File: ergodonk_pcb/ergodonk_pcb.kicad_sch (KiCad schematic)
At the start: 134 parts, among them J1 AudioJack4, Q1 TIP120, SW0 SW_PUSH_LED, SW08_RH10 SW_PUSH_LED, SW1 SW_PUSH_LED, SW10 SW_PUSH_LED, SW11 SW_PUSH_LED, SW12 SW_PUSH_LED, SW13 SW_PUSH_LED, SW14 SW_PUSH_LED, SW15 SW_PUSH_LED, SW16 SW_PUSH_LED, SW17 SW_PUSH_LED, SW18_RH10 SW_PUSH_LED, SW2 SW_PUSH_LED, SW20 SW_PUSH_LED, SW21 SW_PUSH_LED, SW22 SW_PUSH_LED, SW23 SW_PUSH_LED, SW24 SW_PUSH_LED, SW25 SW_PUSH_LED, SW26 SW_PUSH_LED, SW27 SW_PUSH_LED, SW28_RH10 SW_PUSH_LED, SW3 SW_PUSH_LED, SW30 SW_PUSH_LED, SW31 SW_PUSH_LED, SW32 SW_PUSH_LED, SW33 SW_PUSH_LED, SW34 SW_PUSH_LED, SW35 SW_PUSH_LED, SW36 SW_PUSH_LED, SW37 SW_PUSH_LED, SW38_RH10 SW_PUSH_LED, SW4 SW_PUSH_LED, SW40 SW_PUSH_LED, SW42 SW_PUSH_LED, SW43 SW_PUSH_LED, SW44 SW_PUSH_LED, SW45 SW_PUSH_LED, SW46 SW_PUSH_LED, SW47 SW_PUSH_LED, SW48_RH10 SW_PUSH_LED, SW5 SW_PUSH_LED, SW50 SW_PUSH_LED, SW51 SW_PUSH_LED, SW52 SW_PUSH_LED, SW53 SW_PUSH_LED, SW54 SW_PUSH_LED, SW55 SW_PUSH_LED, SW56 SW_PUSH_LED, SW57 SW_PUSH_LED, SW58 SW_PUSH_LED, SW6 SW_PUSH_LED, SW7 SW_PUSH_LED

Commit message: Removed hand indication pin pin and updated footprints
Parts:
- removed JP6: SolderJumper_3_Open, Keebio-Parts:SolderJumper, symbol Jumper:SolderJumper_3_Open
- D0, D08_RH10, D1, D10, D11, D12, D13, D14, D15, D16, D17, D18_RH10, D2, D20, D21, D22, D23, D24, D25, D26, D27, D28_RH10, D3, D30, D31, D32, D33, D34, D35, D36, D37, D38_RH10, D4, D40, D41, D42, D43, D44, D45, D46, D47, D48_RH10, D5, D50, D51, D52, D53, D54, D55, D56, D57, D58, D6, D7: footprint ergodonk_kicad_library:D3_TH_SMD_v3_ergodonk -> ergodonk_kicad_library:D_SOD-123_DO-35_Hybrid_DoubleSided
- Q1: footprint Package_TO_SOT_THT:TO-220-3_Vertical -> Package_TO_SOT_THT:TO-220-3_Horizontal_TabDown
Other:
- note added: "Todo: Unbridge the handed pin jumper before double sided Add 2mm border Rewire for ProMicro footprint RH trackball Double sided RH/LH Add LEDs Graphics Mouse bites Stabalizer holes Improve solenoid graphics Refactor key row/columns to put 00 in upper right for easier double sided Make Diode holes bigger Add breakaway diode bender jig, like on Corne_light v1"
- note removed: "Split hand pin. Left is high, right would be low."
- note removed: "Todo: Unbridge the handed pin jumper before double sided Add 2mm border Rewire for ProMicro footprint RH trackball Double sided RH/LH Add LEDs Graphics Mouse bites Stabalizer holes Improve solenoid graphics Refactor key row/columns to put 00 in upper right for easier double sided"

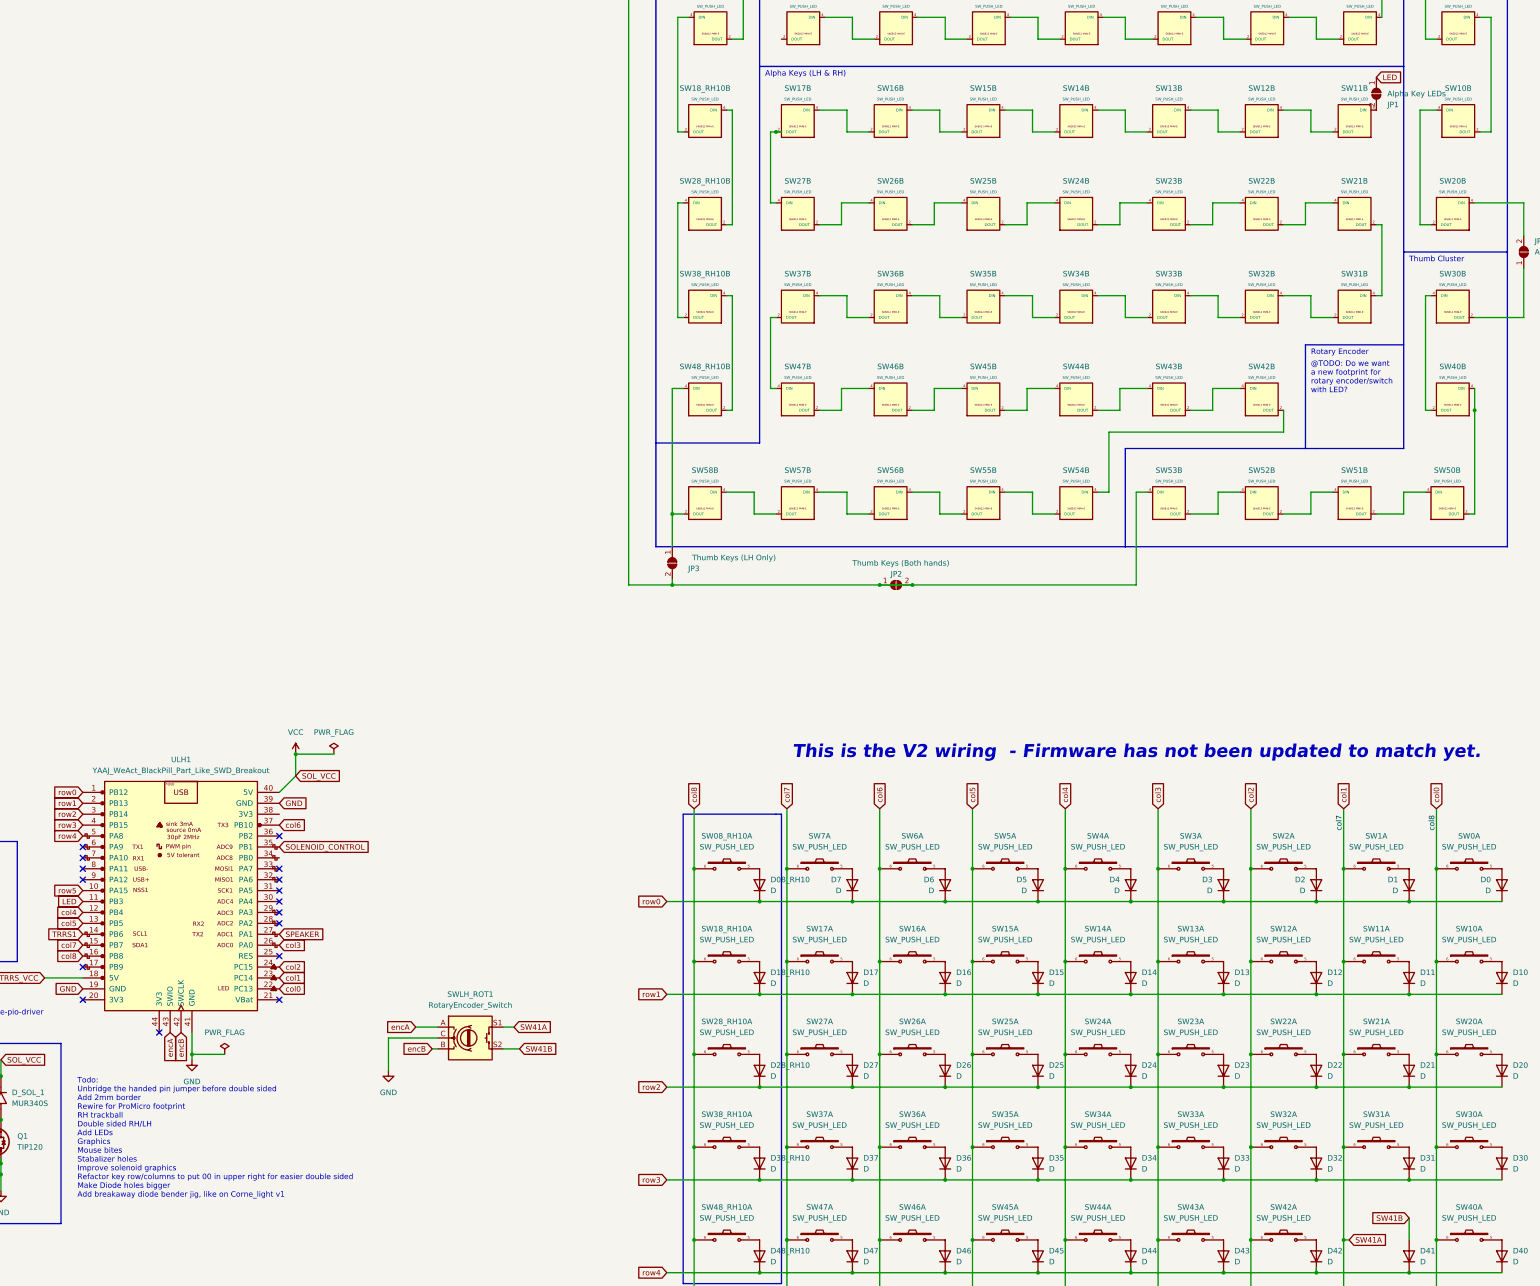
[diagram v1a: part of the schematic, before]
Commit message: Increased default net width and removed LED initial jumper
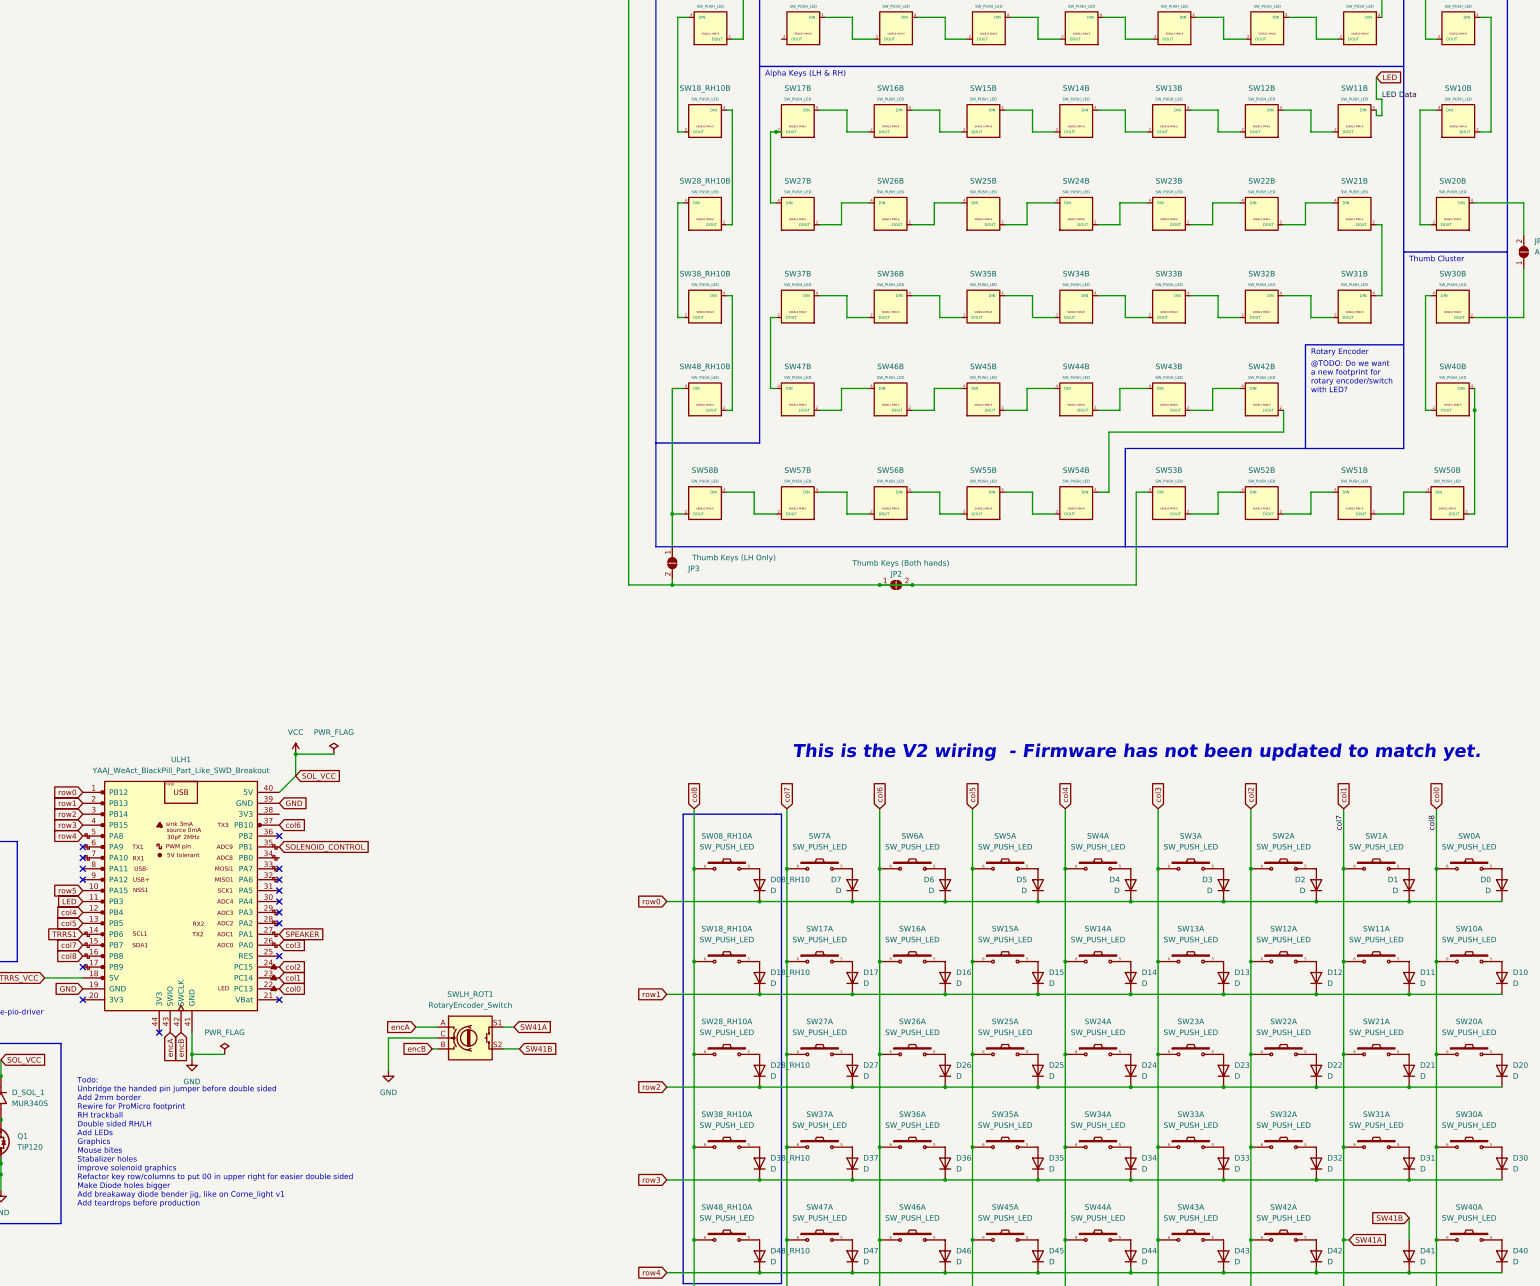
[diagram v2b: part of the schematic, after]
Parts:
- removed JP1: Alpha Key LEDs, Keebio-Parts:solder_jumper, symbol Jumper:SolderJumper_2_Open
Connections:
- net LED: now also SW11.4 (DIN)
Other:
- note added: "Todo: Unbridge the handed pin jumper before double sided Add 2mm border Rewire for ProMicro footprint RH trackball Double sided RH/LH Add LEDs Graphics Mouse bites Stabalizer holes Improve solenoid graphics Refactor key row/columns to put 00 in upper right for easier double sided Make Diode holes bigger Add breakaway diode bender jig, like on Corne_light v1 Add teardrops before production"
- note removed: "Todo: Unbridge the handed pin jumper before double sided Add 2mm border Rewire for ProMicro footprint RH trackball Double sided RH/LH Add LEDs Graphics Mouse bites Stabalizer holes Improve solenoid graphics Refactor key row/columns to put 00 in upper right for easier double sided Make Diode holes bigger Add breakaway diode bender jig, like on Corne_light v1"
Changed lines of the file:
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@@
     (stroke (width 0) (type default))
   )
+  (wire (pts (xy 373.38 -133.35) (xy 373.38 -129.54))
+    (stroke (width 0) (type default))
+  )
   (wire (pts (xy 299.72 45.72) (xy 299.72 31.75))
     (stroke (width 0) (type default))
@@
     (stroke (width 0) (type default))
   )
+  (wire (pts (xy 372.11 -133.35) (xy 372.11 -138.43))
+    (stroke (width 0) (type default))
+  )
   (wire (pts (xy 335.28 -82.55) (xy 335.28 -87.63))
     (stroke (width 0) (type default))
@@
     (stroke (width 0) (type default))
   )
+  (wire (pts (xy 373.38 -129.54) (xy 372.11 -129.54))
+    (stroke (width 0) (type default))
+  )
   (polyline (pts (xy 55.88 67.31) (xy 55.88 39.37))
     (stroke (width 0) (type default))
@@
     (stroke (width 0) (type default))
   )
+  (wire (pts (xy 372.11 -129.54) (xy 372.11 -130.81))
+    (stroke (width 0) (type default))
+  )
   (wire (pts (xy 290.83 -104.14) (xy 290.83 -109.22))
     (stroke (width 0) (type default))
@@
     (stroke (width 0) (type default))
   )
+  (wire (pts (xy 373.38 -133.35) (xy 372.11 -133.35))
+    (stroke (width 0) (type default))
+  )
   (wire (pts (xy 372.11 -104.14) (xy 373.38 -104.14))
     (stroke (width 0) (type default))
@@
     (effects (font (size 3 3) (thickness 0.6) bold italic) (justify left bottom))
   )
-  (text "Todo:\nUnbridge the handed pin jumper before double sided\nAdd 2mm border\nRewire for ProMicro footprint\nRH trackball\nDouble sided RH/LH\nAdd LEDs\nGraphics\nMouse bites\nStabalizer holes\nImprove solenoid graphics\nRefactor key row/columns to put 00 in upper right for easier double sided\nMake Diode holes bigger\nAdd breakaway diode bender jig, like on Corne_light v1\n\n"
+  (text "Todo:\nUnbridge the handed pin jumper before double sided\nAdd 2mm border\nRewire for ProMicro footprint\nRH trackball\nDouble sided RH/LH\nAdd LEDs\nGraphics\nMouse bites\nStabalizer holes\nImprove solenoid graphics\nRefactor key row/columns to put 00 in upper right for easier double sided\nMake Diode holes bigger\nAdd breakaway diode bender jig, like on Corne_light v1\nAdd teardrops before production\n"
     (at 69.85 124.46 0)
     (effects (font (size 1.27 1.27)) (justify left bottom))
@@
     (effects (font (size 1.27 1.27)) (justify left bottom))
   )
+  (label "LED Data" (at 373.38 -133.35 0) (fields_autoplaced)
+    (effects (font (size 1.27 1.27)) (justify left bottom))
+  )
   (label "col8" (at 386.08 36.83 90) (fields_autoplaced)
     (effects (font (size 1.27 1.27)) (justify left bottom))
@@
         )
       )
-    )
-  )
-  (symbol (lib_id "Jumper:SolderJumper_2_Open") (at 372.11 -134.62 270) (unit 1)
-    (in_bom yes) (on_board yes) (dnp no)
-    (property "Reference" "JP1" (at 374.65 -132.08 90)
-      (effects (font (size 1.27 1.27)) (justify left))
-    )
-    (property "Value" "Alpha Key LEDs" (at 374.65 -134.62 90)
-      (effects (font (size 1.27 1.27)) (justify left))
-    )
-    (property "Footprint" "Keebio-Parts:solder_jumper" (at 372.11 -134.62 0)
-      (effects (font (size 1.27 1.27)) hide)
-    )
-    (property "Datasheet" "~" (at 372.11 -134.62 0)
-      (effects (font (size 1.27 1.27)) hide)
-    )
-    (pin "1")
-    (pin "2")
-    (instances
-      (project "ergodonk_pcb"
-        (path "/ed1aaf15-4e1f-4159-b371-d99b3fb972ad"
-          (reference "JP1") (unit 1)
-        )
-      )

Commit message: Switch footprint refactor Hotswop outline replaced and rounded Hotswap pad numbering aligned per side Hotswap pad traces and vias added miniE led footprint with doublesided vias added Schematics updated PCB updated
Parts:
- SW0, SW1, SW10, SW11, SW12, SW13, SW14, SW15, SW16, SW17, SW2, SW20, SW21, SW22, SW23, SW24, SW25, SW26, SW3, SW30, SW31, SW32, SW33, SW34, SW35, SW36, SW4, SW40, SW42, SW43, SW44, SW45, SW46, SW5, SW50, SW54, SW55, SW56, SW6, SW7: footprint ergodonk_kicad_library:CherryMX_DoubleSided_Hotswap_miniE -> ergodonk_kicad_library:V2_CherryMX_DoubleSided_Hotswap_miniE
- SW08_RH10: footprint ergodonk_kicad_library:CherryMX_DoubleSided_Hotswap_miniE_2u_RH_ONLY -> ergodonk_kicad_library:V2_CherryMX_DoubleSided_Hotswap_miniE_2u_RH_ONLY
- SW18_RH10, SW38_RH10: footprint ergodonk_kicad_library:CherryMX_DoubleSided_Hotswap_miniE_1u_RH_ONLY -> ergodonk_kicad_library:V2_CherryMX_DS_Hotswap_miniE_1U_SEED_RH
- SW27: footprint ergodonk_kicad_library:CherryMX_DoubleSided_Hotswap_miniE_1.5u_LH_1u_RH -> ergodonk_kicad_library:V2_CherryMX_DoubleSided_Hotswap_miniE_1.5u_LH_1u_RH
- SW28_RH10: footprint ergodonk_kicad_library:CherryMX_DoubleSided_Hotswap_miniE_1.5u_RH_ONLY -> ergodonk_kicad_library:V2_CherryMX_DoubleSided_Hotswap_miniE_1.5u_RH_ONLY
- SW37: footprint ergodonk_kicad_library:CherryMX_DoubleSided_Hotswap_miniE_1.75u_LH_1u_RH -> ergodonk_kicad_library:V2_CherryMX_DoubleSided_Hotswap_miniE_1.75u_LH_1u_RH
- SW47: footprint ergodonk_kicad_library:CherryMX_DoubleSided_Hotswap_miniE_2.25u_LH_2.75u_RH -> ergodonk_kicad_library:V2_CherryMX_DoubleSided_Hotswap_miniE_2.25u_LH_2.75u_RH
- SW48_RH10: footprint ergodonk_kicad_library:CherryMX_DoubleSided_Hotswap_miniE_2.25u_LH_ONLY -> ergodonk_kicad_library:V2_CherryMX_DoubleSided_Hotswap_miniE_2.25u_LH_ONLY
- SW51, SW52: footprint ergodonk_kicad_library:CherryMX_DoubleSided_Hotswap_miniE_2u_Vertical -> ergodonk_kicad_library:V2_CherryMX_DoubleSided_Hotswap_miniE_2u_Vertical
- SW53: footprint ergodonk_kicad_library:CherryMX_DoubleSided_Hotswap_miniE_1.25u_Vertical -> ergodonk_kicad_library:V2_CherryMX_DoubleSided_Hotswap_miniE_1.25u_Vertical
- SW57, SW58: footprint ergodonk_kicad_library:CherryMX_DoubleSided_Hotswap_miniE_1.25u -> ergodonk_kicad_library:V2_CherryMX_DoubleSided_Hotswap_miniE_1.25u

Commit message: Rewired to 2040 begun Rewired rows and columns Added net names for rows and columns. Removed Key 00 to make room for PI Added OLED Added SDA/SDL breakout for optional Pimoroni
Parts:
- removed D0: D, ergodonk_kicad_library:D_SOD-123_DO-35_Hybrid_DoubleSided, symbol Device:D
- removed J1: AudioJack4, kbd:MJ-4PP-9, symbol kbd:MJ-4PP-9
- removed SW0: SW_PUSH_LED, ergodonk_kicad_library:V2_CherryMX_DoubleSided_Hotswap_miniE, symbol SofleKeyboard:SW_PUSH_LED
- added J10: TRRS Double Sided, Resistor_SMD:R_1206_3216Metric_Pad1.30x1.75mm_HandSolder, symbol Ergodonk_symbols:TRRS_TX_to_RX_Doublesided_Crossover
- added J12: Conn_01x04_Socket, symbol Connector:Conn_01x04_Socket
- added JP10: Jumper_2_Open, symbol Jumper:Jumper_2_Open
- added OL10: OLED, symbol kbd:OLED
- added R12: R, symbol Device:R
- added R2: 10k, Resistor_SMD:R_1206_3216Metric_Pad1.30x1.75mm_HandSolder, symbol Device:R
- added U10: Pico, RPi_Pico:RPi_Pico_SMD_TH, symbol MCU_RaspberryPi_and_Boards:Pico
- R1: value 1.5K -> 5k6; footprint kbd:R -> Resistor_SMD:R_1206_3216Metric_Pad1.30x1.75mm_HandSolder
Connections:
- net GND: now also J10.3 (RING1), J10.6 (RING1), J12.4 (Pin_4), OL10.4 (GND), R2.2, U10.13 (GND), U10.18 (GND), U10.23 (GND), U10.28 (GND), U10.3 (GND), U10.38 (GND), U10.8 (GND); no longer ULH1.39 (GND)
- net LED: now also U10.29 (GPIO22); no longer ULH1.11 (PB3)
- net SOLENOID_CONTROL: now also U10.27 (GPIO21); no longer ULH1.35 (PB1)
- net SPEAKER: now also U10.26 (GPIO20); no longer ULH1.27 (PA1)
- net SW41A: now also U10.12 (GPIO9); no longer SW17.6, SW27.6, SW37.6, SW47.6, SW57.6, SW7.6, ULH1.15 (PB7), ULH1.23 (PC14)
- net VCC: now also J10.4 (TIP), J10.5 (TIP), JP10.1 (A), OL10.3 (VCC), R12.2
- net col0: now also U10.11 (GPIO8); no longer SW08_RH10.6, SW18_RH10.6, SW28_RH10.6, SW38_RH10.6, SW48_RH10.6, SW58.6, ULH1.16 (PB8), ULH1.22 (PC13)
- net col2: now also U10.14 (GPIO10); no longer ULH1.24 (PC15)
- net col3: now also U10.15 (GPIO11); no longer ULH1.26 (PA0)
- net col4: now also U10.16 (GPIO12); no longer ULH1.12 (PB4)
- net col5: now also U10.17 (GPIO13); no longer ULH1.13 (PB5)
- net col6: now also U10.19 (GPIO14); no longer ULH1.37 (PB10)
- net encA: now also U10.32 (GPIO27_ADC1); no longer ULH1.43 (SWIO)
- net encB: now also U10.31 (GPIO26_ADC0); no longer ULH1.42 (SWCLK)
- net row0: now also U10.4 (GPIO2); no longer ULH1.1 (PB12)
- net row1: now also U10.5 (GPIO3); no longer ULH1.2 (PB13)
- net row2: now also U10.6 (GPIO4); no longer ULH1.3 (PB14)
- net row3: now also U10.7 (GPIO5); no longer ULH1.4 (PB15)
- net row4: now also U10.9 (GPIO6); no longer ULH1.5 (PA8)
- net row5: now also U10.10 (GPIO7); no longer ULH1.10 (PA15)
- net VBUS: now reaches R1.1
- net at JP5.1 (A): now also SW10.2 (DOUT)
- net TRRS1: no longer names the net of ULH1.14 (PB6)
- net TRRS1: no longer R1.2
- net TRRS_VCC: no longer names the net of ULH1.18 (5V)
- new net: J12.3 (Pin_3), JP10.2 (B), R12.1
- new net OLED 1: U10.25 (GPIO19)
- new net OLED 2: U10.24 (GPIO18)
- new net RX: J10.1 (SLEEVE), J10.7 (RING2), U10.2 (GPIO1)
- new net SCL: OL10.2 (SCL)
- new net SDA: J12.1 (Pin_1), J12.2 (Pin_2), OL10.1 (SDA)
- new net TX: J10.2 (RING2), J10.8 (SLEEVE), U10.1 (GPIO0)
- new net col7: SW17.6, SW27.6, SW37.6, SW47.6, SW57.6, SW7.6, U10.20 (GPIO15)
- new net col8: SW08_RH10.6, SW18_RH10.6, SW28_RH10.6, SW38_RH10.6, SW48_RH10.6, SW58.6, U10.34 (GPIO28_ADC2)
- new net vbus_sense: R1.2, R2.1
- no-connect marks 18 -> 17
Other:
- note added: "Add aux keys to another section?"
- note added: "OLED (Chain to pimaroni for sharing bus?)"
- note added: "Pimaroni Tie in (Additional Resistor?)"
- note added: "Rotary Knob"
- note added: "Speaker! (WTF not!)"
- note added: "Todo: pimaroni tie in additional pim resistor Figure out VCC on Pico Figure out vbus_sense Make new symbol for double sided TRRS Cutouts for picon on PCB Rewire for ProMicro footprint RH trackball Double sided RH/LH Add LEDs Graphics Mouse bites Stabalizer holes Improve solenoid graphics Refactor key row/columns to put 00 in upper right for easier double sided Make Diode holes bigger Add breakawa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"
- note added: "Whats the max led power draw"
- note removed: "Note! This is only needed with the blackpill, as RP2040 uses an internal pull-up resistor for half-duplex https://docs.qmk.fm/#/serial_driver?id=the-pio-driver"
- note removed: "Pull up resistor required for half duplex. Only needed on one hand."
- note removed: "This is the V2 wiring - Firmware has not been updated to match yet."
- note removed: "Todo: Unbridge the handed pin jumper before double sided Add 2mm border Rewire for ProMicro footprint RH trackball Double sided RH/LH Add LEDs Graphics Mouse bites Stabalizer holes Improve solenoid graphics Refactor key row/columns to put 00 in upper right for easier double sided Make Diode holes bigger Add breakaway diode bender jig, like on Corne_light v1 Add teardrops before production"
- moved on the sheet: LS1, SWLH_ROT1

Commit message: Updated PCB from schematicatic, diode cleanup
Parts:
- SWLH_ROT1: footprint ergodonk_kicad_library:RotaryEncoder_EC11_with_MX_hotswap_v2 -> ergodonk_kicad_library:RotaryEncoder_EC11_ergodonk_variant
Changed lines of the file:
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@@
       (effects (font (size 1.27 1.27)))
     )
-    (property "Footprint" "ergodonk_kicad_library:RotaryEncoder_EC11_with_MX_hotswap_v2" (at 161.29 144.526 0)
+    (property "Footprint" "ergodonk_kicad_library:RotaryEncoder_EC11_ergodonk_variant" (at 161.29 144.526 0)
       (effects (font (size 1.27 1.27)) hide)
     )

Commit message: Simplified LED config to mirror Keebio Sync Rev3
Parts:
- removed JP2: Thumb Keys (Both hands), Keebio-Parts:solder_jumper, symbol Jumper:SolderJumper_2_Open
- removed JP4: Aux Keys, Keebio-Parts:solder_jumper, symbol Jumper:SolderJumper_2_Open
- removed JP5: F Keys, Keebio-Parts:solder_jumper, symbol Jumper:SolderJumper_2_Open
- JP3: value Thumb Keys (LH Only) -> LH remaining keys
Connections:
- net GND: no longer SW40.4 (DIN), SW50.2 (DOUT)
- net LED: now also U10.24 (GPIO18); no longer U10.29 (GPIO22)
- net OLED 1: now also U10.22 (GPIO17); no longer U10.25 (GPIO19)
- net OLED 2: now also U10.21 (GPIO16); no longer U10.24 (GPIO18)
- net at SW20.4 (DIN): now also SW30.2 (DOUT)
- net at SW10.2 (DOUT): now also SW1.4 (DIN)
- new net: SW40.4 (DIN), SW50.2 (DOUT)
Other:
- note added: "LED's 1) Based on Keebio Sync rev3, we can put in all these LED's if we limit brightness Add a jumper if you want to make the LH snap off for assymetry."
- note removed: "Add aux keys to another section?"
- note removed: "LED's 1) Jumper blocking all LED's for testing - can remove in final 2) All LED's are in series - you can only turn them on sequentially: a. Alphas (Jumper 1) b. Thumb clusters (LH 1 & 2 & 3, RH 1 & 3) c. Aux keys (LH 1 & 2 & 3 & 4, RH 1 & 3 & 4) d. F Keys (LH 1 & 2 & 3 & 4 & 5, RH 1 & 3 & 4 & 5) 3) Do not install RH only LED's on the Left hand. (Should I dummy proof with another jumper?)"
- note removed: "Whats the max led power draw"
